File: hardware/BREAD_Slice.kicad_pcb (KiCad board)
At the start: 2 copper layers, 70 x 100 mm, 83 parts, among them J1 I2C_01x04, J2 Conn_01x10_Female, J4 Conn_01x02, J5 Conn_01x02, J6 Conn_01x02, J7 Conn_01x02, U2 CD74HC4053E, U3 MIC5225-3.3YM5-TR, U4 MAX31856, U5 MAX31856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

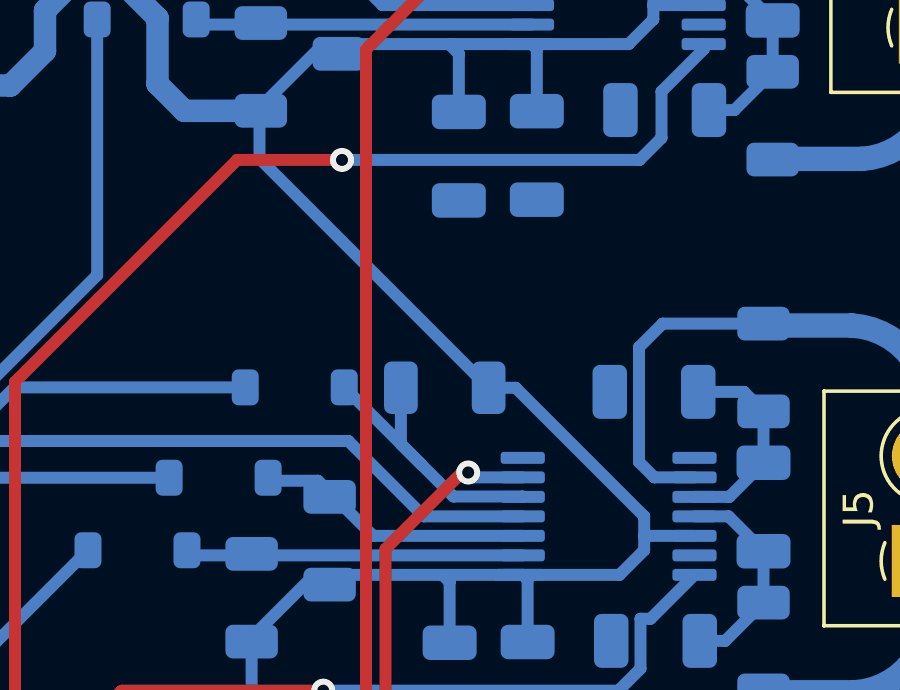
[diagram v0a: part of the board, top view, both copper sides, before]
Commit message: hw: fix erc and drc errors; need to double check the diode and levelshift ic pathes can be independently toggled before prod
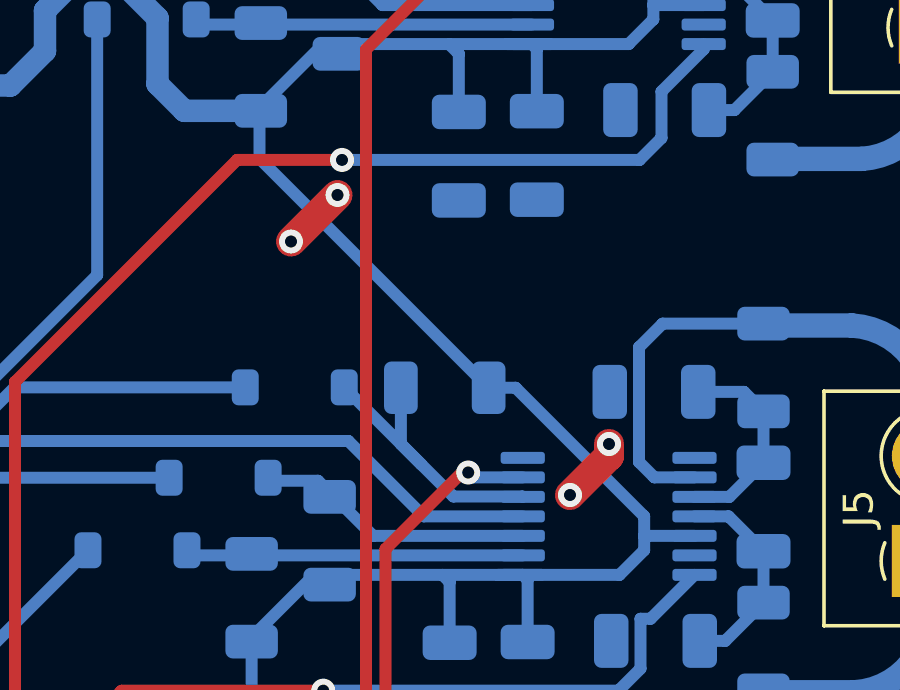
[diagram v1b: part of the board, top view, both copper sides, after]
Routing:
- net GND: track 19.2 -> 23.6 mm, vias 14 -> 18
